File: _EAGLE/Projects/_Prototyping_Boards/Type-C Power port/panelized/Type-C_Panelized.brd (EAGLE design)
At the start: 100 x 100 mm, 40 parts, among them J1 TYPE-C-31-M-17, J10 TYPE-C-31-M-17, J11 TYPE-C-31-M-17, J12 TYPE-C-31-M-17, J13 TYPE-C-31-M-17, J14 TYPE-C-31-M-17, J15 TYPE-C-31-M-17, J16 TYPE-C-31-M-17, J17 TYPE-C-31-M-17, J18 TYPE-C-31-M-17, J19 TYPE-C-31-M-17, J2 TYPE-C-31-M-17, J20 TYPE-C-31-M-17, J3 TYPE-C-31-M-17, J4 TYPE-C-31-M-17, J5 TYPE-C-31-M-17, J6 TYPE-C-31-M-17, J7 TYPE-C-31-M-17, J8 TYPE-C-31-M-17, J9 TYPE-C-31-M-17

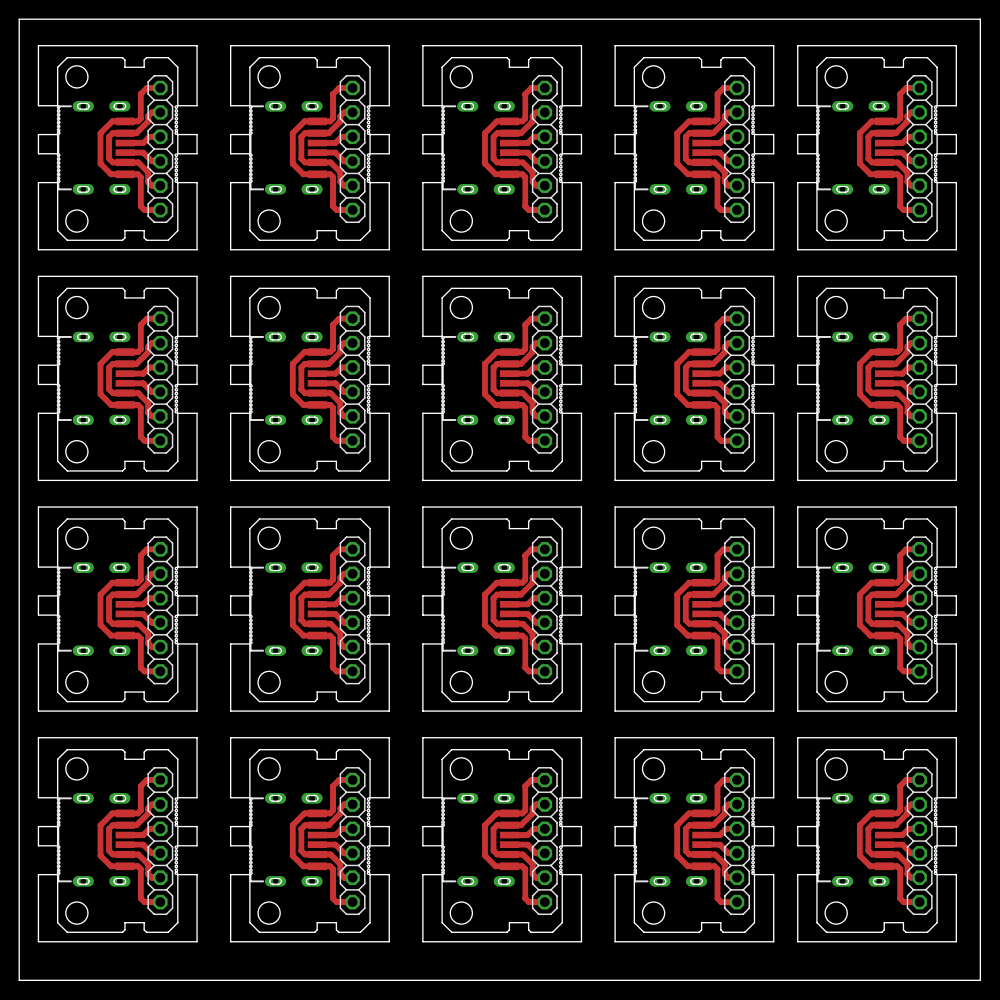
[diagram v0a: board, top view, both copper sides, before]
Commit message: Type-C power port PCB panelization V1.1.0
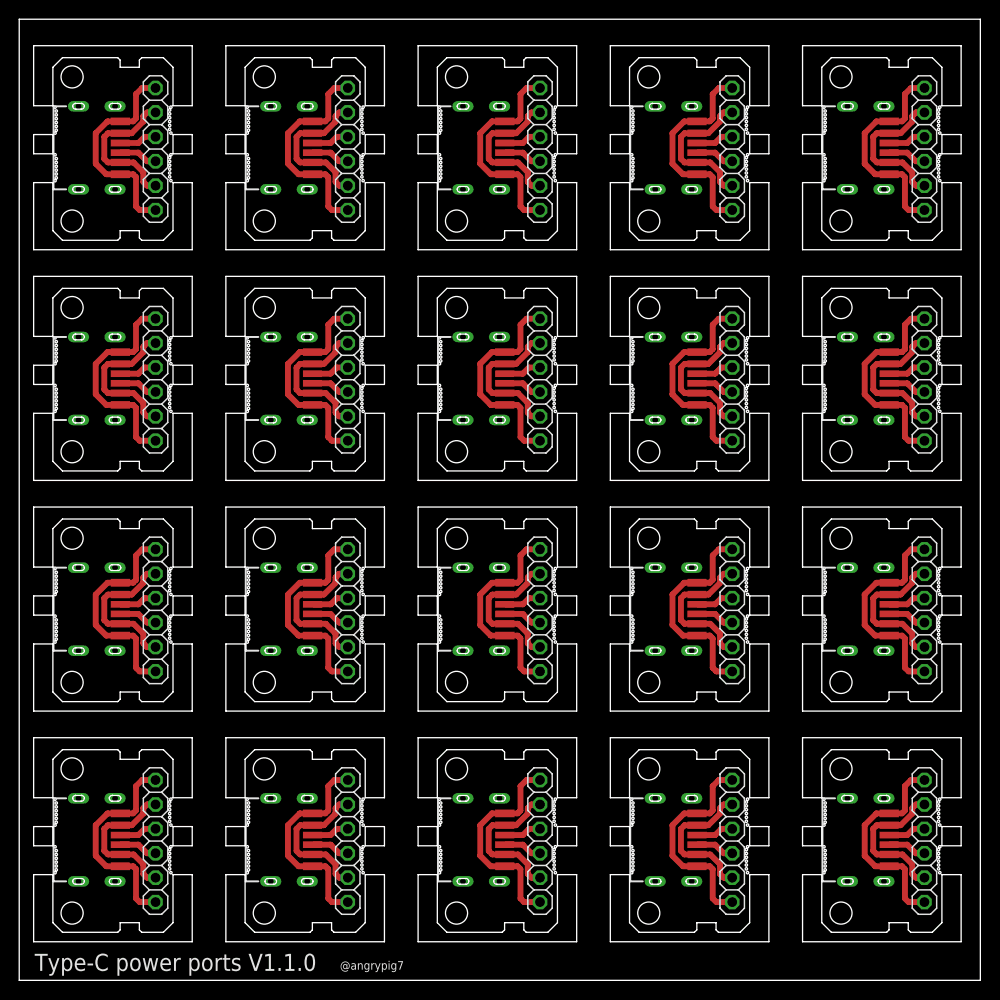
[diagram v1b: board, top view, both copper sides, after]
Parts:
- moved J1 0.50 mm to (0.12, 76.6)
- moved J10 0.50 mm to (80.1, 52.6)
- moved J11 0.50 mm to (0.12, 28.6)
- moved J12 0.50 mm to (20.1, 28.6)
- moved J13 0.50 mm to (40.1, 28.6)
- moved J14 0.50 mm to (60.1, 28.6)
- moved J15 0.50 mm to (80.1, 28.6)
- moved J16 0.50 mm to (0.12, 4.62)
- moved J17 0.50 mm to (20.1, 4.62)
- moved J18 0.50 mm to (40.1, 4.62)
- moved J19 0.50 mm to (60.1, 4.62)
- moved J2 0.50 mm to (20.1, 76.6)
- moved J20 0.50 mm to (80.1, 4.62)
- moved J3 0.50 mm to (40.1, 76.6)
- moved J4 0.50 mm to (60.1, 76.6)
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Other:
- outline, holes or cut-outs redrawn
- board text added: "@angrypig7"
- board text added: "Type-C power ports V1.1.0"
